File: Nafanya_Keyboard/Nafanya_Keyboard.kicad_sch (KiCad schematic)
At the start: 46 parts, among them J1 KEYBOARD_TO_NAFANYA, SW1 1, SW10 T, SW11 A, SW12 S, SW13 D, SW14 F, SW15 G, SW16 CAPS_SHIFT, SW17 Z, SW18 X, SW19 C, SW2 2, SW20 V, SW21 6, SW22 Y, SW23 H, SW24 B, SW25 7, SW26 U, SW27 J, SW28 N, SW29 8, SW3 3, SW30 I, SW31 K, SW32 M, SW33 9, SW34 O, SW35 L, SW36 SYMBOL_SHIFT, SW37 0, SW38 P, SW39 ENTER, SW4 4, SW40 BREAK_SPACE, SW41 RESET, SW5 5, SW6 Q, SW7 W, SW8 E, SW9 R

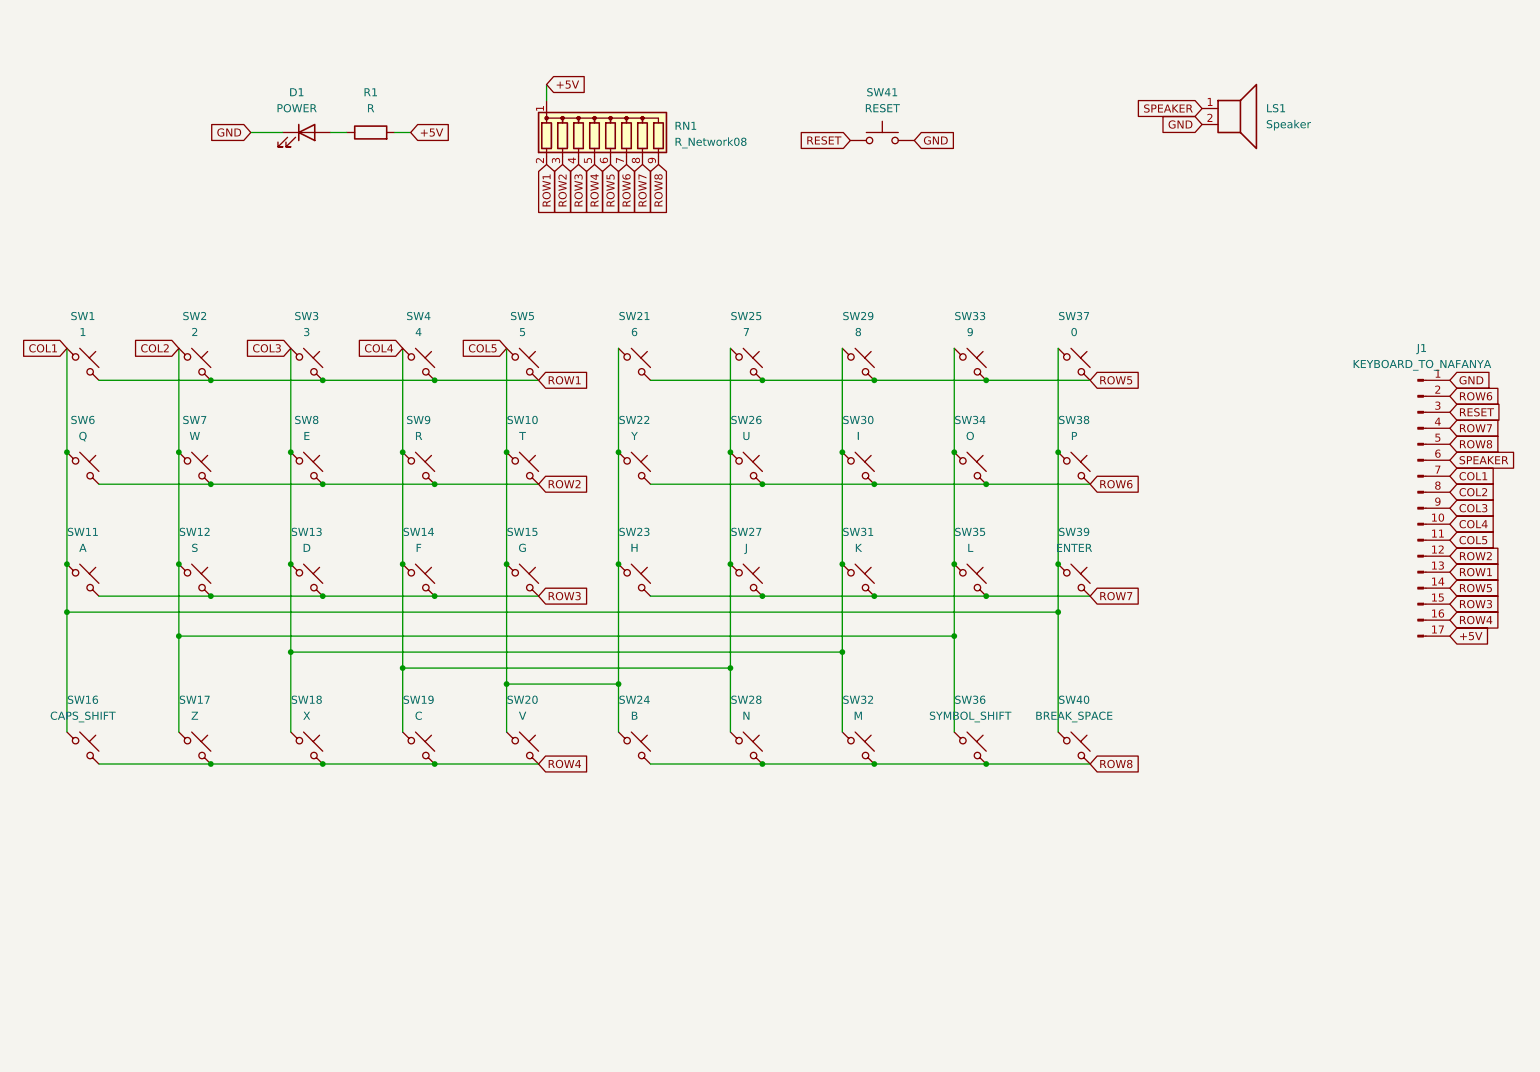
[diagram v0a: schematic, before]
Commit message: Adding mounting holes
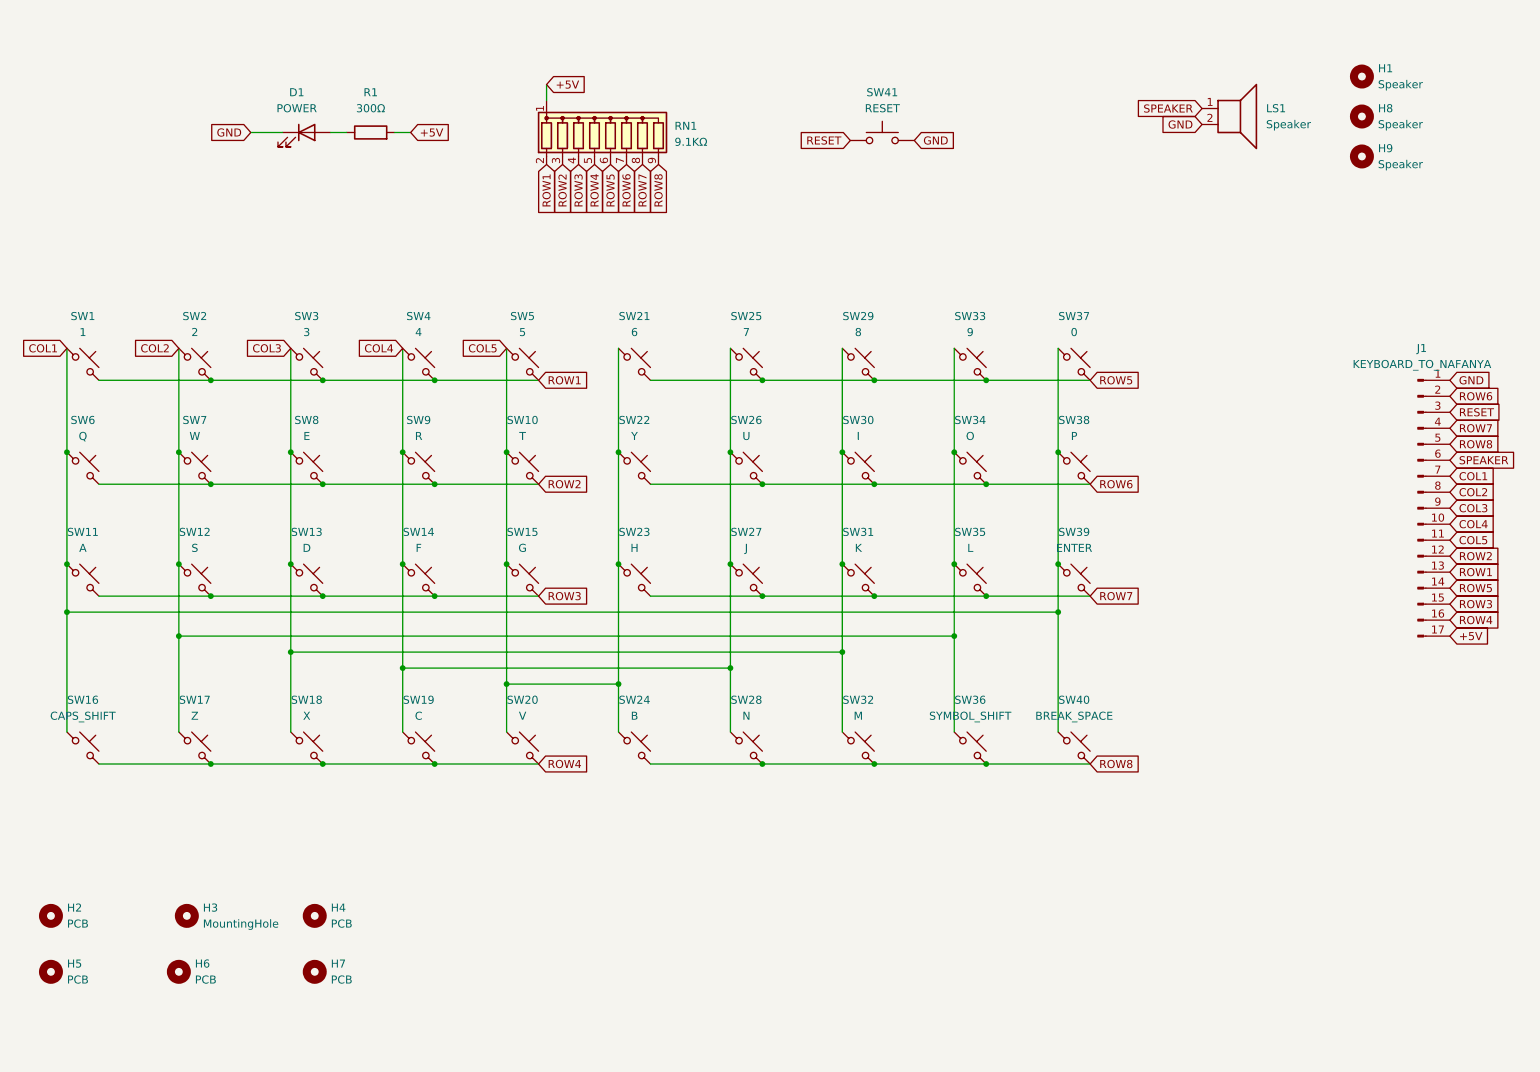
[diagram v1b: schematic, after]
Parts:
- added H1, H8, H9: Speaker, symbol Mechanical:MountingHole
- added H2, H4, H5, H6, H7: PCB, symbol Mechanical:MountingHole
- added H3: MountingHole, symbol Mechanical:MountingHole
- R1: value R -> 300Ω
- RN1: value R_Network08 -> 9.1KΩ

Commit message: PCB started
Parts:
- D1: footprint (none) -> LED_THT:LED_D5.0mm
- H1, H2, H4, H5, H6, H7, H8, H9: footprint (none) -> MountingHole:MountingHole_3.2mm_M3
- H3: value MountingHole -> PCB; footprint (none) -> MountingHole:MountingHole_3.2mm_M3
- J1: footprint (none) -> Connector_PinHeader_2.54mm:PinHeader_1x17_P2.54mm_Horizontal
- LS1: footprint (none) -> Connector_PinHeader_2.54mm:PinHeader_1x02_P2.54mm_Vertical
- R1: footprint (none) -> Resistor_THT:R_Axial_DIN0207_L6.3mm_D2.5mm_P7.62mm_Horizontal
- SW1, SW10, SW11, SW12, SW13, SW14, SW15, SW16, SW17, SW18, SW19, SW2, SW20, SW21, SW22, SW23, SW24, SW25, SW26, SW27, SW28, SW29, SW3, SW30, SW31, SW32, SW33, SW34, SW35, SW36, SW37, SW38, SW39, SW4, SW40, SW41, SW5, SW6, SW7, SW8, SW9: footprint (none) -> Button_Switch_THT:SW_PUSH_6mm_H8.5mm
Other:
- moved on the sheet: H2, H3, H4, H5, H7, SW10, SW11, SW12, SW13, SW14, SW15, SW16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

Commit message: Initial keyboard PCB designed
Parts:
- removed H9: Speaker, MountingHole:MountingHole_3.2mm_M3, symbol Mechanical:MountingHole
- removed J1: KEYBOARD_TO_NAFANYA, Connector_PinHeader_2.54mm:PinHeader_1x17_P2.54mm_Horizontal, symbol Connector:Conn_01x17_Pin
- added J1: Speaker/Reset/Power, Connector_PinHeader_2.54mm:PinHeader_1x04_P2.54mm_Horizontal, symbol Connector:Conn_01x04_Pin
- added J2: Columns, Connector_PinHeader_2.54mm:PinHeader_1x05_P2.54mm_Horizontal, symbol Connector:Conn_01x05_Pin
- added J3: Rows, Connector_PinHeader_2.54mm:PinHeader_1x08_P2.54mm_Horizontal, symbol Connector:Conn_01x08_Pin
- added J4: Faceplate GND, Connector_PinSocket_2.54mm:PinSocket_1x01_P2.54mm_Vertical, symbol Connector:Conn_01x01_Pin
- renumbered SW37 to SW10, SW6 to SW11, SW7 to SW12, SW8 to SW13, SW9 to SW14, SW10 to SW15, SW22 to SW16, SW26 to SW17, SW30 to SW18, SW34 to SW19, SW38 to SW20, SW11 to SW21, SW12 to SW22, SW13 to SW23, SW14 to SW24, SW15 to SW25, SW23 to SW26, SW31 to SW28, SW35 to SW29, SW39 to SW30, SW16 to SW31, SW17 to SW32, SW18 to SW33, SW19 to SW34, SW20 to SW35, SW24 to SW36, SW28 to SW37, SW32 to SW38, SW36 to SW39, SW21 to SW6, SW25 to SW7, SW29 to SW8, SW33 to SW9
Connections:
- net +5V: now also J1.4 (Pin_4)
- net COL1: now also J2.1 (Pin_1)
- net COL2: now also J2.2 (Pin_2)
- net COL3: now also J2.3 (Pin_3)
- net COL4: now also J2.4 (Pin_4)
- net COL5: now also J2.5 (Pin_5)
- net GND: now also J1.2 (Pin_2), J4.1 (Pin_1)
- net RESET: now also J1.3 (Pin_3)
- net ROW1: now also J3.1 (Pin_1)
- net ROW2: now also J3.2 (Pin_2)
- net ROW3: now also J3.3 (Pin_3)
- net ROW4: now also J3.4 (Pin_4)
- net ROW5: now also J3.5 (Pin_5)
- net ROW6: now also J3.6 (Pin_6)
- net ROW7: now also J3.7 (Pin_7)
- net ROW8: now also J3.8 (Pin_8)
- net SPEAKER: now also J1.1 (Pin_1)

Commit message: Finalised layout
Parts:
- removed RN1: 9.1KΩ, Resistor_THT:R_Array_SIP9, symbol Device:R_Network08
- added R2, R3, R4, R5, R6, R7, R8, R9: 10KΩ, Resistor_THT:R_Axial_DIN0207_L6.3mm_D2.5mm_P7.62mm_Horizontal, symbol Device:R
- SW1, SW10, SW11, SW12, SW13, SW14, SW15, SW16, SW17, SW18, SW19, SW2, SW20, SW21, SW22, SW23, SW24, SW25, SW26, SW27, SW28, SW29, SW3, SW30, SW31, SW32, SW33, SW34, SW35, SW36, SW37, SW38, SW39, SW4, SW40, SW5, SW6, SW7, SW8, SW9: footprint Button_Switch_THT:SW_PUSH_6mm_H8.5mm -> Button_Switch_THT:SW_PUSH_6mm
- SW41: value RESET -> RESET/СБРОС; footprint Button_Switch_THT:SW_PUSH_6mm_H8.5mm -> Button_Switch_THT:SW_PUSH_6mm
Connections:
- net +5V: now also J1.1 (Pin_1), R2.1, R3.1, R4.1, R5.1, R6.1, R7.1, R8.1, R9.1; no longer J1.4 (Pin_4)
- net ROW1: now also R2.2
- net ROW2: now also R3.2
- net ROW3: now also R4.2
- net ROW4: now also R5.2
- net ROW5: now also R6.2
- net ROW6: now also R7.2
- net ROW7: now also R8.2
- net ROW8: now also R9.2
- net SPEAKER: now also J1.4 (Pin_4); no longer J1.1 (Pin_1)
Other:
- moved on the sheet: H1, H2, H3, H4, H5, H6, H7, H8, LS1, SW41
